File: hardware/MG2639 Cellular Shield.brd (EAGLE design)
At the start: 53.3 x 74.9 mm, 63 parts, among them Q1 MMBT2222A, U1 SPX29302, U2 TXB0104, U3 MG2639V3

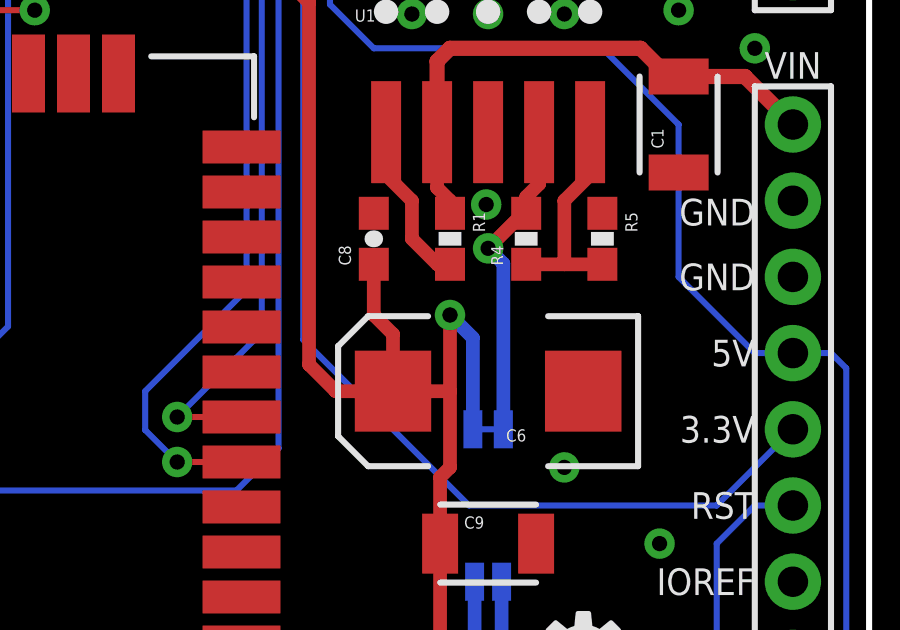
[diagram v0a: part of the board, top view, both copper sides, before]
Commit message: Adding test point to 3.8V bus.
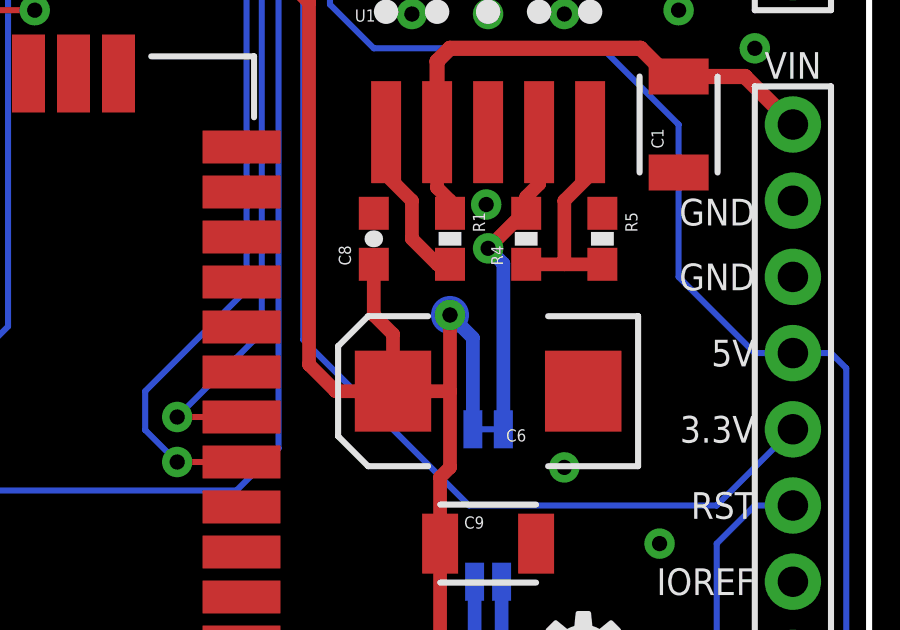
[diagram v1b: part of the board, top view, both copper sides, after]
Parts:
- added TP3: (no value), SparkFun-Passives:PAD.03X.05
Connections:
- net 3.8V: now also TP3.P$1
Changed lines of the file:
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@@
 <element name="SJ9" library="SparkFun-Passives" package="PAD-JUMPER-3-2OF3_NC_BY_TRACE_YES_SILK_FULL_BOX" value="" x="6.35" y="35.56" rot="MR270"/>
 <element name="SJ10" library="SparkFun-Passives" package="PAD-JUMPER-3-2OF3_NC_BY_TRACE_YES_SILK_FULL_BOX" value="" x="6.35" y="29.21" rot="MR270"/>
+<element name="TP3" library="SparkFun-Passives" package="PAD.03X.05" value="" x="39.37" y="30.48" rot="MR0"/>
 </elements>
 <signals>
@@
 <wire x1="39.04" y1="22.86" x2="39.04" y2="18.999" width="0.4572" layer="1"/>
 <wire x1="39.04" y1="18.999" x2="39.37" y2="18.669" width="0.4572" layer="1"/>
+<contactref element="TP3" pad="P$1"/>
 </signal>
 <signal name="N$3">

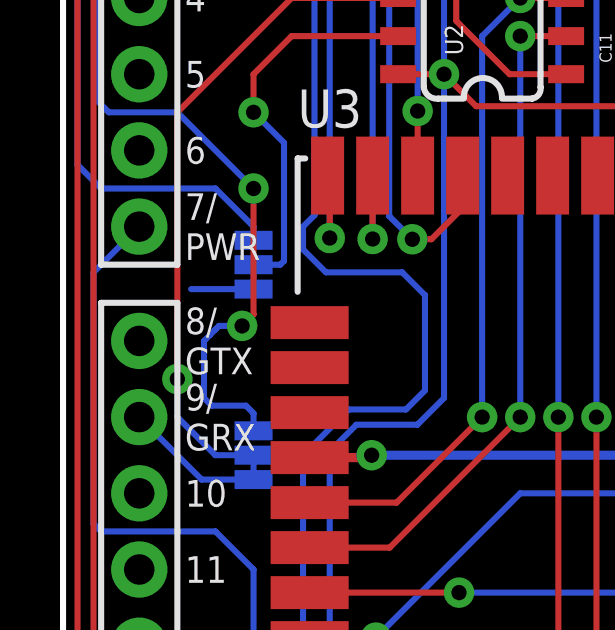
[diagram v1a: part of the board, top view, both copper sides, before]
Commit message: Re-routing GTX-HV to D8 on the Arduino.
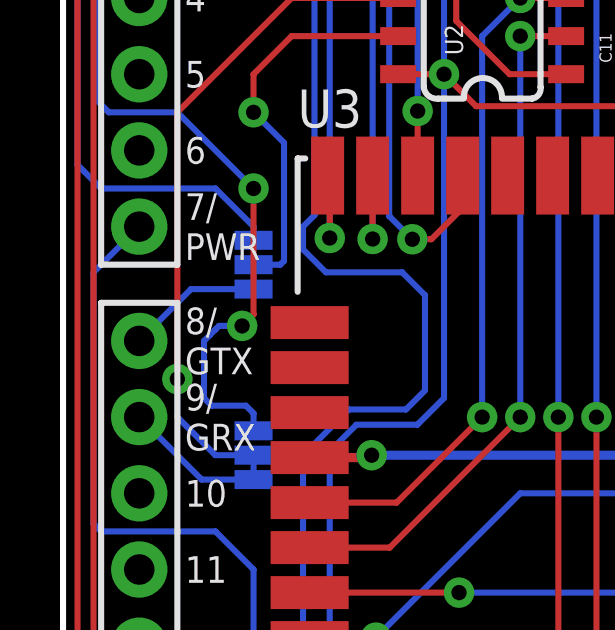
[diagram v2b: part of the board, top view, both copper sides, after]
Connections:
- removed net CELL_RESET: JP3.D6
- removed net JP9: JP3.D8
- net GTX-SOFT: now also JP3.D8
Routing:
- net GTX-SOFT: track 2.08 -> 4.53 mm
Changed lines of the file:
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@@
 <wire x1="23.28" y1="46.57" x2="22.63" y2="47.22" width="0.2032" layer="1"/>
-</signal>
-<signal name="CELL_RESET">
-<contactref element="JP3" pad="D6"/>
 </signal>
 <signal name="GPS_FIX">
@@
 <contactref element="SJ9" pad="3"/>
 <wire x1="6.35" y1="34.7472" x2="4.2672" y2="34.7472" width="0.2032" layer="16"/>
+<contactref element="JP3" pad="D8"/>
+<wire x1="4.2672" y1="34.7472" x2="2.54" y2="33.02" width="0.2032" layer="16"/>
 </signal>
 <signal name="GRX-SOFT">
@@
 <wire x1="4.6228" y1="28.3972" x2="2.54" y2="30.48" width="0.2032" layer="16"/>
 </signal>
-<signal name="JP9">
-<contactref element="JP3" pad="D8"/>
-</signal>
 </signals>

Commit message: Cleaning up nets around Arduino Shield connector (removing stubs).
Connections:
- removed net A1: JP3.A1
- removed net A2: JP3.A2
- removed net A3: JP3.A3
- removed net A4: JP3.A4
- removed net A5: JP3.A5
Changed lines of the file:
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@@
 <wire x1="8.255" y1="50.165" x2="8.255" y2="56.134" width="0.2032" layer="16"/>
-</signal>
-<signal name="A1">
-<contactref element="JP3" pad="A1"/>
-</signal>
-<signal name="A2">
-<contactref element="JP3" pad="A2"/>
-</signal>
-<signal name="A3">
-<contactref element="JP3" pad="A3"/>
-</signal>
-<signal name="A4">
-<contactref element="JP3" pad="A4"/>
-</signal>
-<signal name="A5">
-<contactref element="JP3" pad="A5"/>
 </signal>
 <signal name="3.8V">

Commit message: Switching GPS fix indicator LED to yellow.
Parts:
- D2: value BLUE -> YELLOW
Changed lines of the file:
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@@
 <attribute name="PROD_ID" value="RES-07856" x="24.13" y="45.72" size="1.778" layer="27" font="vector" ratio="15" rot="R90" display="off"/>
-</element>
-<element name="D2" library="SparkFun-LED" package="LED-1206" value="BLUE" x="26.67" y="45.72" rot="R90">
-<attribute name="PROD_ID" value="DIO-09911" x="26.67" y="45.72" size="1.778" layer="27" font="vector" ratio="15" rot="R90" display="off"/>
 </element>
 <element name="R8" library="SparkFun-Resistors" package="0603-RES" value="1K" x="29.21" y="45.72" rot="R90">
@@
 <element name="SJ10" library="SparkFun-Passives" package="PAD-JUMPER-3-2OF3_NC_BY_TRACE_YES_SILK_FULL_BOX" value="" x="6.35" y="29.21" rot="MR270"/>
 <element name="TP3" library="SparkFun-Passives" package="PAD.03X.05" value="" x="39.37" y="30.48" rot="MR0"/>
+<element name="D2" library="SparkFun-LED" package="LED-1206" value="YELLOW" x="26.67" y="45.72" rot="R90">
+<attribute name="PROD_ID" value="DIO-00820" x="26.67" y="45.72" size="1.778" layer="27" font="vector" ratio="15" rot="R90" display="off"/>
+</element>
 </elements>
 <signals>
@@
 <signal name="GPS_FIX">
 <contactref element="U3" pad="22"/>
-<contactref element="D2" pad="A"/>
 <via x="28.2956" y="43.4848" extent="1-16" drill="0.508"/>
 <wire x1="22.479" y1="27.94" x2="15.24" y2="27.94" width="0.2032" layer="16"/>
@@
 <wire x1="24.638" y1="42.418" x2="25.7048" y2="43.4848" width="0.2032" layer="16"/>
 <wire x1="28.2956" y1="43.4848" x2="25.7048" y2="43.4848" width="0.2032" layer="16"/>
+<contactref element="D2" pad="A"/>
 </signal>
 <signal name="N$9">
 <contactref element="R8" pad="2"/>
-<contactref element="D2" pad="C"/>
 <wire x1="26.67" y1="47.22" x2="27.71" y2="47.22" width="0.2032" layer="1"/>
 <wire x1="29.21" y1="46.57" x2="28.36" y2="46.57" width="0.2032" layer="1"/>
 <wire x1="28.36" y1="46.57" x2="27.71" y2="47.22" width="0.2032" layer="1"/>
+<contactref element="D2" pad="C"/>
 </signal>
 <signal name="VDDIO">

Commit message: moved board fiducial
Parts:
- moved FID2 13.0 mm to (39.4, 72.1)
